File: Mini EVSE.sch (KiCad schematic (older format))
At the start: 55 parts, among them IC2 IRM-03-5, IC3 ATMEGA328PB-AU, IC4 TMR1-0522, IC5 SI8261BAC-C-IP, J10 M, J2 AC IN, J3 AC OUT, J4 ICP, J5 SWITCH, J6 PILOTS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

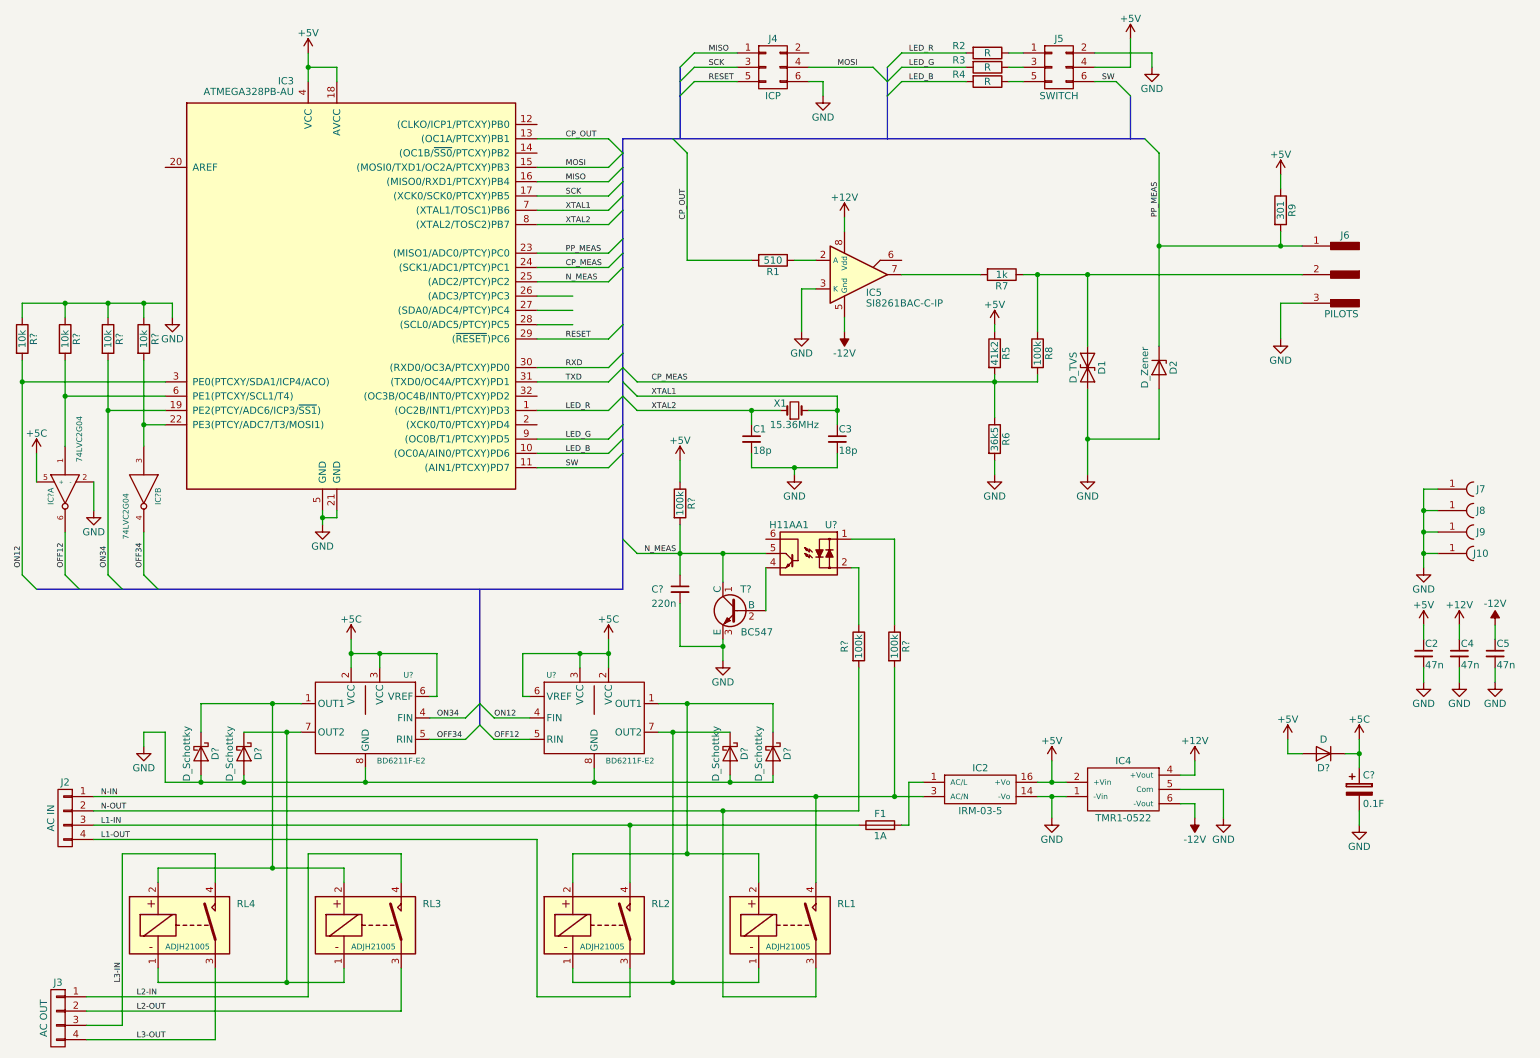
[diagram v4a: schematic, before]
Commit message: Adding neutral contact failure detection and ground detection
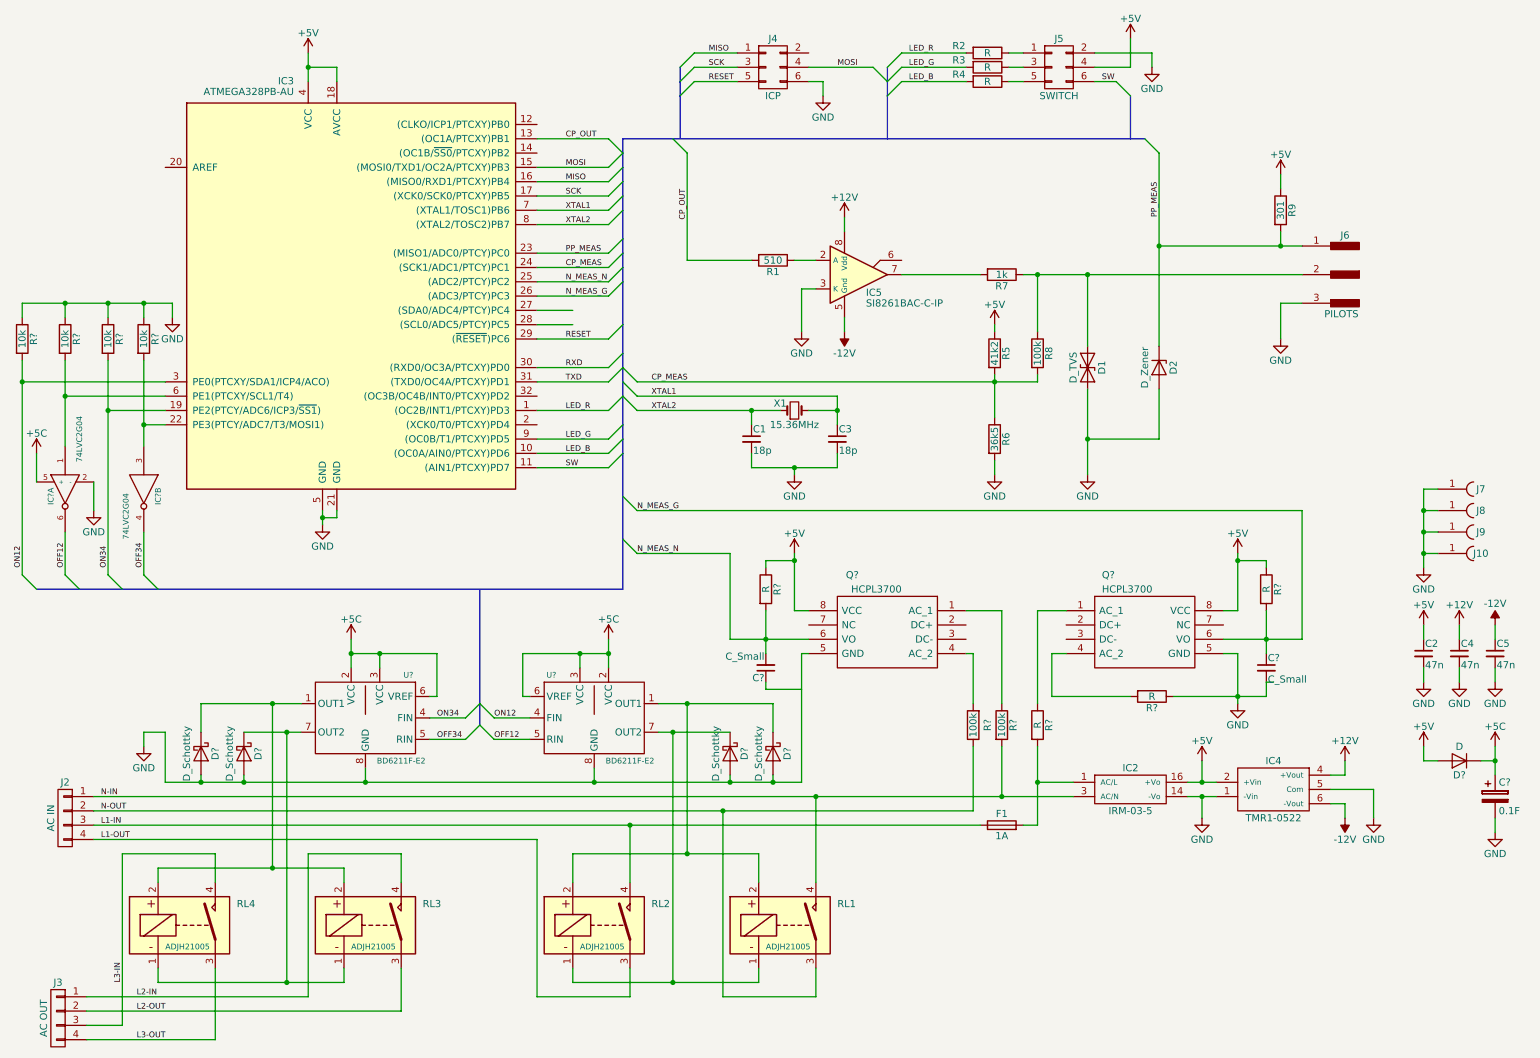
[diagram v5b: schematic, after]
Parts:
- removed C?: 220n, symbol C_Small
- removed R?: 100k, symbol R
- removed T?: BC547, TO_SOT_Packages_THT:TO-92_Molded_Narrow, symbol BC547
- removed U?: H11AA1, Housings_DIP:DIP-6_W7.62mm_SMD, symbol H11AA1
- added C? (x2): C_Small, symbol C_Small
- added Q? (x2): HCPL3700, DIP762W56P254L966H508Q8N, symbol HCPL3700
- added R? (x4): R, symbol R
- RL1, RL2, RL3, RL4: footprint Relays_THT:Relay_SPST-NO_OMRON-G5Q -> SamacSys_Parts:ADJH21005
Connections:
- net +5V: now also Q?.8 (VCC), Q?.8 (VCC), R?.1, R?.1
- net GND: now also C?.2, Q?.5 (GND), Q?.5 (GND), R?.1
- net N-OUT: now also R?.1; no longer R?.2
- net at F1.2, IC2.1 (AC/L): now also R?.2
- net N_MEAS_G: now reaches IC3.26 ((ADC3/PTCY)PC3)
- net N_MEAS_G: now also C?.1, Q?.6 (VO), R?.2
- net at R?.1: now also Q?.1 (AC_1)
- net N_MEAS renamed N_MEAS_N
- net N_MEAS_N: now also C?.2, Q?.6 (VO), R?.2
- new net: Q?.4 (AC_2), R?.2 (x2)
- new net: Q?.1 (AC_1), R?.1
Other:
- moved on the sheet: C?, D?, F1, IC2, IC4, R?

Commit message: Add some footprints
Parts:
- C6, C7: renamed from C?; footprint (none) -> Miscellaneous:C_Disc_D5.1mm_W3.2mm_P5.08mm
- D3, D4, D5, D6: renamed from D?; footprint (none) -> Diodes_THT:D_DO-35_SOD27_P7.62mm_Horizontal
- D7: renamed from D?; footprint (none) -> Diodes_THT:D_DO-35_SOD27_P7.62mm_Horizontal; symbol D -> D_Schottky
- IC1: renamed from IC?; footprint (none) -> TO_SOT_Packages_SMD:SOT-23-6_Handsoldering
- IC4: footprint (none) -> Miscellaneous:Recom_1x05_Pitch2.54mm
- IC6, IC7: renamed from U?; footprint (none) -> SamacSys_Parts:SOIC127P620X160-8N
- IC8, IC9: renamed from Q?; footprint DIP762W56P254L966H508Q8N -> SamacSys_Parts:DIP762W56P254L966H508Q8N
- J2, J3: footprint (none) -> SamacSys_Parts:1792245
- R10, R11, R12, R13, R14, R15, R16, R17, R18, R19: renamed from R?; footprint (none) -> Miscellaneous:R_Axial_DIN0207_L6.3mm_D2.5mm_P10.16mm_Horizontal
- gave numbers to parts that had none: 1

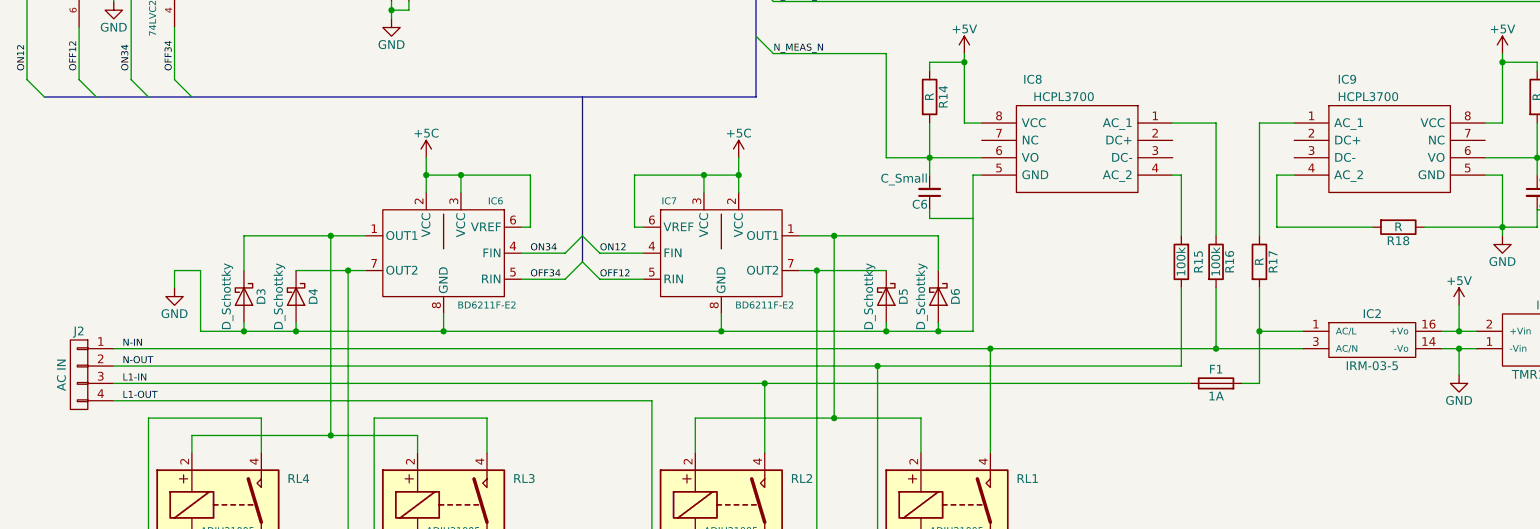
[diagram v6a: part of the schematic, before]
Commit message: - Switching to SMD - Starting PCB layout
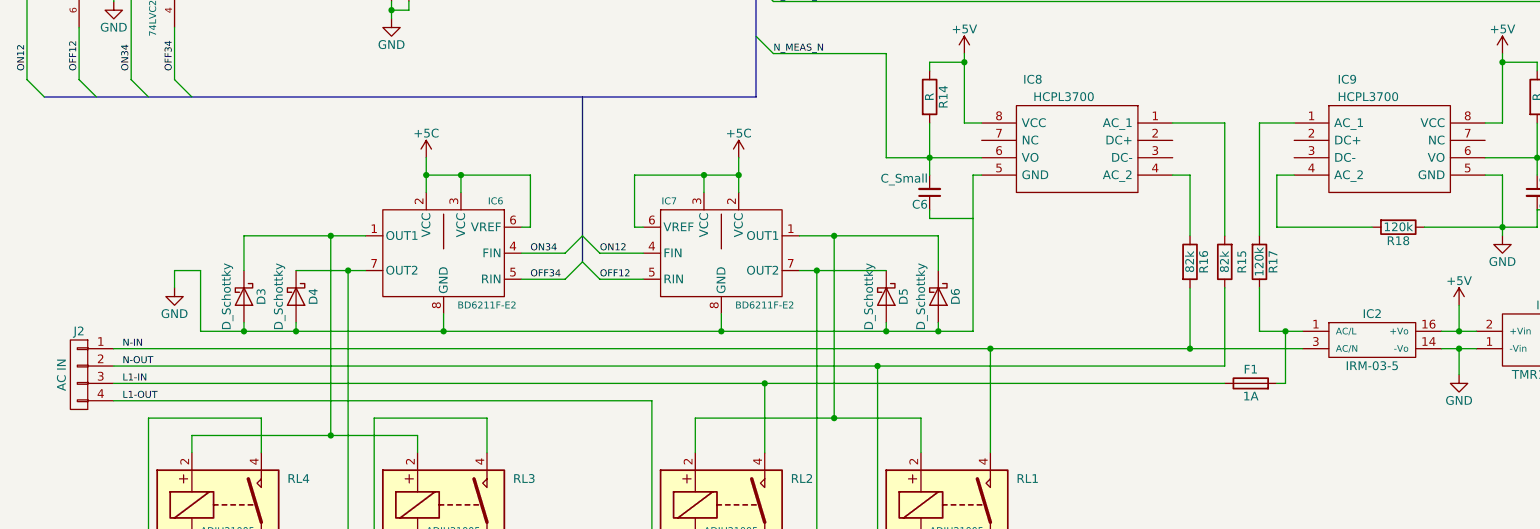
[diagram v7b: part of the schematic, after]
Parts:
- C8: footprint (none) -> Capacitors_THT:CP_Radial_D12.5mm_P5.00mm
- IC8, IC9: footprint SamacSys_Parts:DIP762W56P254L966H508Q8N -> Housings_DIP:SMDIP-8_W7.62mm
- R1, R10, R11, R12, R13, R14, R19, R2, R3, R4, R5, R6, R7, R8, R9: footprint Miscellaneous:R_Axial_DIN0207_L6.3mm_D2.5mm_P10.16mm_Horizontal -> Resistors_SMD:R_1206_HandSoldering
- R15, R16: value 100k -> 82k; footprint Miscellaneous:R_Axial_DIN0207_L6.3mm_D2.5mm_P10.16mm_Horizontal -> Resistors_SMD:R_0805_HandSoldering
- R17, R18: value R -> 120k; footprint Miscellaneous:R_Axial_DIN0207_L6.3mm_D2.5mm_P10.16mm_Horizontal -> Resistors_SMD:R_2010_HandSoldering
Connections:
- net at F1.2, IC2.1 (AC/L): now also R17.1; no longer R17.2
- net at R16.1: now also IC8.4 (AC_2); no longer IC8.1 (AC_1)
- net at R15.2: now also IC8.1 (AC_1); no longer IC8.4 (AC_2)
- net at IC9.1 (AC_1): now also R17.2; no longer R17.1
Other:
- moved on the sheet: F1, R15, R16
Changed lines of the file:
@@
 F 0 "R1" V 5980 2250 50  0000 C CNN
 F 1 "510" V 5900 2250 50  0000 C CNN
-F 2 "Miscellaneous:R_Axial_DIN0207_L6.3mm_D2.5mm_P10.16mm_Horizontal" V 5830 2250 50  0001 C CNN
+F 2 "Resistors_SMD:R_1206_HandSoldering" V 5830 2250 50  0001 C CNN
 F 3 "" H 5900 2250 50  0001 C CNN
 	1    5900 2250
@@
 F 0 "R7" V 7580 2350 50  0000 C CNN
 F 1 "1k" V 7500 2350 50  0000 C CNN
-F 2 "Miscellaneous:R_Axial_DIN0207_L6.3mm_D2.5mm_P10.16mm_Horizontal" V 7430 2350 50  0001 C CNN
+F 2 "Resistors_SMD:R_1206_HandSoldering" V 7430 2350 50  0001 C CNN
 F 3 "" H 7500 2350 50  0001 C CNN
 	1    7500 2350
@@
 F 0 "R8" V 7830 2900 50  0000 C CNN
 F 1 "100k" V 7750 2900 50  0000 C CNN
-F 2 "Miscellaneous:R_Axial_DIN0207_L6.3mm_D2.5mm_P10.16mm_Horizontal" V 7680 2900 50  0001 C CNN
+F 2 "Resistors_SMD:R_1206_HandSoldering" V 7680 2900 50  0001 C CNN
 F 3 "" H 7750 2900 50  0001 C CNN
 	1    7750 2900
@@
 F 0 "R5" V 7530 2900 50  0000 C CNN
 F 1 "41k2" V 7450 2900 50  0000 C CNN
-F 2 "Miscellaneous:R_Axial_DIN0207_L6.3mm_D2.5mm_P10.16mm_Horizontal" V 7380 2900 50  0001 C CNN
+F 2 "Resistors_SMD:R_1206_HandSoldering" V 7380 2900 50  0001 C CNN
 F 3 "" H 7450 2900 50  0001 C CNN
 	1    7450 2900
@@
 F 0 "R6" V 7530 3500 50  0000 C CNN
 F 1 "36k5" V 7450 3500 50  0000 C CNN
-F 2 "Miscellaneous:R_Axial_DIN0207_L6.3mm_D2.5mm_P10.16mm_Horizontal" V 7380 3500 50  0001 C CNN
+F 2 "Resistors_SMD:R_1206_HandSoldering" V 7380 3500 50  0001 C CNN
 F 3 "" H 7450 3500 50  0001 C CNN
 	1    7450 3500
@@
 F 0 "R9" V 9530 1900 50  0000 C CNN
 F 1 "301" V 9450 1900 50  0000 C CNN
-F 2 "Miscellaneous:R_Axial_DIN0207_L6.3mm_D2.5mm_P10.16mm_Horizontal" V 9380 1900 50  0001 C CNN
+F 2 "Resistors_SMD:R_1206_HandSoldering" V 9380 1900 50  0001 C CNN
 F 3 "" H 9450 1900 50  0001 C CNN
 	1    9450 1900
@@
 F 0 "R2" V 7350 600 50  0000 C CNN
 F 1 "R" V 7400 800 50  0000 C CNN
-F 2 "Miscellaneous:R_Axial_DIN0207_L6.3mm_D2.5mm_P10.16mm_Horizontal" V 7330 800 50  0001 C CNN
+F 2 "Resistors_SMD:R_1206_HandSoldering" V 7330 800 50  0001 C CNN
 F 3 "" H 7400 800 50  0001 C CNN
 	1    7400 800
@@
 F 0 "R3" V 7350 700 50  0000 C CNN
 F 1 "R" V 7400 900 50  0000 C CNN
-F 2 "Miscellaneous:R_Axial_DIN0207_L6.3mm_D2.5mm_P10.16mm_Horizontal" V 7330 900 50  0001 C CNN
+F 2 "Resistors_SMD:R_1206_HandSoldering" V 7330 900 50  0001 C CNN
 F 3 "" H 7400 900 50  0001 C CNN
 	1    7400 900
@@
 F 0 "R4" V 7350 800 50  0000 C CNN
 F 1 "R" V 7400 1000 50  0000 C CNN
-F 2 "Miscellaneous:R_Axial_DIN0207_L6.3mm_D2.5mm_P10.16mm_Horizontal" V 7330 1000 50  0001 C CNN
+F 2 "Resistors_SMD:R_1206_HandSoldering" V 7330 1000 50  0001 C CNN
 F 3 "" H 7400 1000 50  0001 C CNN
 	1    7400 1000
@@
 L Fuse F1
 U 1 1 59A72C88
-P 7500 6200
-F 0 "F1" V 7580 6200 50  0000 C CNN
-F 1 "1A" V 7425 6200 50  0000 C CNN
-F 2 "Fuse_Holders_and_Fuses:Fuseholder_Fuse_TR5_Littlefuse-No560_No460" V 7430 6200 50  0001 C CNN
-F 3 "" H 7500 6200 50  0001 C CNN
-	1    7500 6200
+P 7700 6200
+F 0 "F1" V 7780 6200 50  0000 C CNN
+F 1 "1A" V 7625 6200 50  0000 C CNN
+F 2 "Fuse_Holders_and_Fuses:Fuseholder_Fuse_TR5_Littlefuse-No560_No460" V 7630 6200 50  0001 C CNN
+F 3 "" H 7700 6200 50  0001 C CNN
+	1    7700 6200
 	0    -1   -1   0
 $EndComp
@@
 	6200 7400 6200 7200
 Wire Wire Line
-	7500 6000 7500 5650
+	7350 6000 7350 5650
 Connection ~ 6200 6000
 Wire Wire Line
@@
 	5550 7400 6200 7400
 Wire Wire Line
-	1150 6200 7350 6200
+	1150 6200 7550 6200
 Wire Wire Line
 	4900 6200 4900 6600
 Wire Wire Line
-	1150 6100 7300 6100
+	1150 6100 7550 6100
 Connection ~ 4900 6200
 Wire Wire Line
@@
 L R R16
 U 1 1 5B662721
-P 7500 5500
-F 0 "R16" V 7580 5500 50  0000 C CNN
-F 1 "100k" V 7500 5500 50  0000 C CNN
-F 2 "Miscellaneous:R_Axial_DIN0207_L6.3mm_D2.5mm_P10.16mm_Horizontal" V 7430 5500 50  0001 C CNN
-F 3 "" H 7500 5500 50  0001 C CNN
-	1    7500 5500
-	1    0    0    -1
-$EndComp
-Wire Wire Line
-	7500 4700 7500 5350
+P 7350 5500
+F 0 "R16" V 7430 5500 50  0000 C CNN
+F 1 "82k" V 7350 5500 50  0000 C CNN
+F 2 "Resistors_SMD:R_0805_HandSoldering" V 7280 5500 50  0001 C CNN
+F 3 "" H 7350 5500 50  0001 C CNN
+	1    7350 5500
+	1    0    0    -1
+$EndComp
+Wire Wire Line
+	7350 5000 7350 5350
 $Comp
 L R R15
 U 1 1 5B662BFC
-P 7300 5500
-F 0 "R15" V 7200 5500 50  0000 C CNN
-F 1 "100k" V 7300 5500 50  0000 C CNN
-F 2 "Miscellaneous:R_Axial_DIN0207_L6.3mm_D2.5mm_P10.16mm_Horizontal" V 7230 5500 50  0001 C CNN
-F 3 "" H 7300 5500 50  0001 C CNN
-	1    7300 5500
+P 7550 5500
+F 0 "R15" V 7450 5500 50  0000 C CNN
+F 1 "82k" V 7550 5500 50  0000 C CNN
+F 2 "Resistors_SMD:R_0805_HandSoldering" V 7480 5500 50  0001 C CNN
+F 3 "" H 7550 5500 50  0001 C CNN
+	1    7550 5500
 	-1   0    0    1
 $EndComp
 Wire Wire Line
-	7300 5000 7300 5350
-Wire Wire Line
-	7300 6100 7300 5650
+	7550 4700 7550 5350
+Wire Wire Line
+	7550 6100 7550 5650
 Connection ~ 5550 6100
 Wire Wire Line
@@
 F 0 "R10" V 730 2800 50  0000 C CNN
 F 1 "10k" V 650 2800 50  0000 C CNN
-F 2 "Miscellaneous:R_Axial_DIN0207_L6.3mm_D2.5mm_P10.16mm_Horizontal" V 580 2800 50  0001 C CNN
+F 2 "Resistors_SMD:R_1206_HandSoldering" V 580 2800 50  0001 C CNN
 F 3 "" H 650 2800 50  0001 C CNN
 	1    650  2800
@@
 F 0 "R11" V 1030 2800 50  0000 C CNN
 F 1 "10k" V 950 2800 50  0000 C CNN
-F 2 "Miscellaneous:R_Axial_DIN0207_L6.3mm_D2.5mm_P10.16mm_Horizontal" V 880 2800 50  0001 C CNN
+F 2 "Resistors_SMD:R_1206_HandSoldering" V 880 2800 50  0001 C CNN
 F 3 "" H 950 2800 50  0001 C CNN
 	1    950  2800
@@
 F 0 "R12" V 1330 2800 50  0000 C CNN
 F 1 "10k" V 1250 2800 50  0000 C CNN
-F 2 "Miscellaneous:R_Axial_DIN0207_L6.3mm_D2.5mm_P10.16mm_Horizontal" V 1180 2800 50  0001 C CNN
+F 2 "Resistors_SMD:R_1206_HandSoldering" V 1180 2800 50  0001 C CNN
 F 3 "" H 1250 2800 50  0001 C CNN
 	1    1250 2800
@@
 F 0 "R13" V 1580 2800 50  0000 C CNN
 F 1 "10k" V 1500 2800 50  0000 C CNN
-F 2 "Miscellaneous:R_Axial_DIN0207_L6.3mm_D2.5mm_P10.16mm_Horizontal" V 1430 2800 50  0001 C CNN
+F 2 "Resistors_SMD:R_1206_HandSoldering" V 1430 2800 50  0001 C CNN
 F 3 "" H 1500 2800 50  0001 C CNN
 	1    1500 2800
@@
 Text Label 1500 4400 1    40   ~ 0
 OFF34
-Connection ~ 7500 6000
-Wire Wire Line
-	8000 5900 7750 5900
-Wire Wire Line
-	7750 5650 7750 6200
-Wire Wire Line
-	7750 6200 7650 6200
+Connection ~ 7350 6000
+Wire Wire Line
+	7900 5900 7900 6200
+Wire Wire Line
+	7900 6200 7850 6200
 $Comp
 L CP C8
@@
 F 0 "C8" H 10975 6100 50  0000 L CNN
 F 1 "0.1F" H 10975 5900 50  0000 L CNN
-F 2 "" H 10988 5850 50  0001 C CNN
+F 2 "Capacitors_THT:CP_Radial_D12.5mm_P5.00mm" H 10988 5850 50  0001 C CNN
 F 3 "" H 10950 6000 50  0001 C CNN
 	1    10950 6000
@@
 F 0 "IC8" H 8000 4950 50  0000 L CNN
 F 1 "HCPL3700" H 7700 4850 50  0000 L CNN
-F 2 "SamacSys_Parts:DIP762W56P254L966H508Q8N" H 8200 4800 50  0001 L CNN
+F 2 "Housings_DIP:SMDIP-8_W7.62mm" H 8200 4800 50  0001 L CNN
 F 3 "https://www.mouser.ch/datasheet/2/308/HCPL3700-1301093.pdf" H 8200 4700 50  0001 L CNN
 F 4 "AC/DC to Logic Optocoupler w/Base PDIP8" H 8200 4600 50  0001 L CNN "Description"
@@
 	-1   0    0    -1
 $EndComp
-Wire Wire Line
-	7300 5000 7250 5000
-Wire Wire Line
-	7500 4700 7250 4700
 $Comp
 L HCPL3700 IC9
@@
 F 0 "IC9" H 8200 4950 50  0000 L CNN
 F 1 "HCPL3700" H 8200 4850 50  0000 L CNN
-F 2 "SamacSys_Parts:DIP762W56P254L966H508Q8N" H 8900 4800 50  0001 L CNN
+F 2 "Housings_DIP:SMDIP-8_W7.62mm" H 8900 4800 50  0001 L CNN
 F 3 "https://www.mouser.ch/datasheet/2/308/HCPL3700-1301093.pdf" H 8900 4700 50  0001 L CNN
 F 4 "AC/DC to Logic Optocoupler w/Base PDIP8" H 8900 4600 50  0001 L CNN "Description"
@@
 P 7750 5500
 F 0 "R17" V 7830 5500 50  0000 C CNN
-F 1 "R" V 7750 5500 50  0000 C CNN
-F 2 "Miscellaneous:R_Axial_DIN0207_L6.3mm_D2.5mm_P10.16mm_Horizontal" V 7680 5500 50  0001 C CNN
+F 1 "120k" V 7750 5500 50  0000 C CNN
+F 2 "Resistors_SMD:R_2010_HandSoldering" V 7680 5500 50  0001 C CNN
 F 3 "" H 7750 5500 50  0001 C CNN
 	1    7750 5500
-	1    0    0    -1
+	1    0    0    1
 $EndComp
 $Comp
@@
 P 8550 5300
 F 0 "R18" V 8630 5300 50  0000 C CNN
-F 1 "R" V 8550 5300 50  0000 C CNN
-F 2 "Miscellaneous:R_Axial_DIN0207_L6.3mm_D2.5mm_P10.16mm_Horizontal" V 8480 5300 50  0001 C CNN
+F 1 "120k" V 8550 5300 50  0000 C CNN
+F 2 "Resistors_SMD:R_2010_HandSoldering" V 8480 5300 50  0001 C CNN
 F 3 "" H 8550 5300 50  0001 C CNN
 	1    8550 5300
@@
 	7750 5350 7750 4700
 Wire Wire Line
-	7750 4700 7950 4700
-Wire Wire Line
 	7850 5300 7850 5000
-Wire Wire Line
-	7850 5000 7950 5000
 $Comp
 L GND #PWR033
@@
 F 0 "R19" V 9430 4550 50  0000 C CNN
 F 1 "R" V 9350 4550 50  0000 C CNN
-F 2 "Miscellaneous:R_Axial_DIN0207_L6.3mm_D2.5mm_P10.16mm_Horizontal" V 9280 4550 50  0001 C CNN
+F 2 "Resistors_SMD:R_1206_HandSoldering" V 9280 4550 50  0001 C CNN
 F 3 "" H 9350 4550 50  0001 C CNN
 	1    9350 4550
@@
 F 0 "R14" V 5930 4550 50  0000 C CNN
 F 1 "R" V 5850 4550 50  0000 C CNN
-F 2 "Miscellaneous:R_Axial_DIN0207_L6.3mm_D2.5mm_P10.16mm_Horizontal" V 5780 4550 50  0001 C CNN
+F 2 "Resistors_SMD:R_1206_HandSoldering" V 5780 4550 50  0001 C CNN
 F 3 "" H 5850 4550 50  0001 C CNN
 	1    5850 4550
@@
 Wire Wire Line
 	7850 5300 8400 5300
-Connection ~ 7750 5900
+Connection ~ 7900 5900
+Wire Wire Line
+	7550 4700 7250 4700
+Wire Wire Line
+	7350 5000 7250 5000
+Wire Wire Line
+	7750 5900 8000 5900
+Wire Wire Line
+	7850 5000 7950 5000
+Wire Wire Line
+	7750 4700 7950 4700
+Wire Wire Line
+	7750 5650 7750 5900
 $EndSCHEMATC
